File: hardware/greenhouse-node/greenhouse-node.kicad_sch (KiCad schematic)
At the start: 30 parts, among them J1 Conn_01x12_Male, J2 Conn_01x02_Male, J3 Conn_01x02_Male, J4 Conn_01x02_Male, J5 Conn_01x04_Male, J6 RX_PinHeader_1x04_P2.54mm, J7 TX_PinHeader_1x04_P2.54mm, Q1 BC549C, U1 ATtiny84A-P, U2 L7805, U3 74HC595

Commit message: Swap OE and RCLK
Drive OE low
Fixed missing SRCLR pull-up
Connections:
- net SR_OE: now also U1.6 (PA7); no longer J5.4 (Pin_4), U1.9 (PA4)
- net SR_RCLK: now also J5.4 (Pin_4), U1.9 (PA4); no longer U1.6 (PA7)
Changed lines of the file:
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@@
     (stroke (width 0) (type default) (color 0 0 0 0))
   )
-  (wire (pts (xy 116.84 99.06) (xy 134.62 99.06))
+  (wire (pts (xy 134.62 97.79) (xy 134.62 100.33))
+    (stroke (width 0) (type default) (color 0 0 0 0))
+  )
+  (wire (pts (xy 116.84 106.68) (xy 134.62 106.68))
     (stroke (width 0) (type default) (color 0 0 0 0))
   )
@@
     (stroke (width 0) (type default) (color 0 0 0 0))
   )
-  (wire (pts (xy 123.19 154.94) (xy 130.81 154.94))
+  (wire (pts (xy 123.19 154.94) (xy 133.35 154.94))
     (stroke (width 0) (type default) (color 0 0 0 0))
   )
@@
     (stroke (width 0) (type default) (color 0 0 0 0))
   )
-  (wire (pts (xy 123.19 147.32) (xy 130.81 147.32))
+  (wire (pts (xy 123.19 147.32) (xy 133.35 147.32))
     (stroke (width 0) (type default) (color 0 0 0 0))
   )
@@
     (stroke (width 0) (type default) (color 0 0 0 0))
   )
+  (wire (pts (xy 116.84 99.06) (xy 130.81 99.06))
+    (stroke (width 0) (type default) (color 0 0 0 0))
+  )
   (wire (pts (xy 116.84 104.14) (xy 130.81 104.14))
     (stroke (width 0) (type default) (color 0 0 0 0))
@@
     (stroke (width 0) (type default) (color 0 0 0 0))
   )
-  (wire (pts (xy 134.62 90.17) (xy 134.62 92.71))
-    (stroke (width 0) (type default) (color 0 0 0 0))
-  )
-  (wire (pts (xy 116.84 106.68) (xy 130.81 106.68))
-    (stroke (width 0) (type default) (color 0 0 0 0))
-  )
   (wire (pts (xy 57.15 97.79) (xy 57.15 105.41))
     (stroke (width 0) (type default) (color 0 0 0 0))
@@
     (stroke (width 0) (type default) (color 0 0 0 0))
   )
-  (wire (pts (xy 134.62 97.79) (xy 134.62 99.06))
-    (stroke (width 0) (type default) (color 0 0 0 0))
-  )
   (wire (pts (xy 100.33 52.07) (xy 106.68 52.07))
     (stroke (width 0) (type default) (color 0 0 0 0))
@@
     (stroke (width 0) (type default) (color 0 0 0 0))
   )
-  (wire (pts (xy 123.19 152.4) (xy 130.81 152.4))
+  (wire (pts (xy 123.19 152.4) (xy 133.35 152.4))
     (stroke (width 0) (type default) (color 0 0 0 0))
   )
@@
     (stroke (width 0) (type default) (color 0 0 0 0))
   )
-  (wire (pts (xy 123.19 149.86) (xy 130.81 149.86))
+  (wire (pts (xy 134.62 105.41) (xy 134.62 106.68))
+    (stroke (width 0) (type default) (color 0 0 0 0))
+  )
+  (wire (pts (xy 123.19 149.86) (xy 133.35 149.86))
     (stroke (width 0) (type default) (color 0 0 0 0))
   )
@@
     (effects (font (size 1.27 1.27)) (justify right bottom))
   )
-  (label "SR_SER" (at 130.81 149.86 180)
-    (effects (font (size 1.27 1.27)) (justify right bottom))
-  )
-  (label "SR_OE" (at 130.81 154.94 180)
+  (label "SR_OE" (at 130.81 106.68 180)
+    (effects (font (size 1.27 1.27)) (justify right bottom))
+  )
+  (label "SR_SER" (at 133.35 149.86 180)
+    (effects (font (size 1.27 1.27)) (justify right bottom))
+  )
+  (label "SR_RCLK" (at 133.35 154.94 180)
     (effects (font (size 1.27 1.27)) (justify right bottom))
   )
@@
     (effects (font (size 1.27 1.27)) (justify right bottom))
   )
-  (label "SR_CLK" (at 130.81 152.4 180)
+  (label "SR_RCLK" (at 130.81 99.06 180)
+    (effects (font (size 1.27 1.27)) (justify right bottom))
+  )
+  (label "SR_CLK" (at 133.35 152.4 180)
     (effects (font (size 1.27 1.27)) (justify right bottom))
   )
@@
     (effects (font (size 1.27 1.27)) (justify left bottom))
   )
-  (label "SR_OE" (at 130.81 99.06 180)
-    (effects (font (size 1.27 1.27)) (justify right bottom))
-  )
   (label "RAD_TX" (at 228.6 53.34 0)
     (effects (font (size 1.27 1.27)) (justify left bottom))
@@
     (effects (font (size 1.27 1.27)) (justify right bottom))
   )
-  (label "SR_RCLK" (at 130.81 106.68 180)
-    (effects (font (size 1.27 1.27)) (justify right bottom))
-  )
   (label "LED_Y" (at 152.4 53.34 0)
     (effects (font (size 1.27 1.27)) (justify left bottom))
@@
     (effects (font (size 1.27 1.27)) (justify right bottom))
   )
-  (label "Reset" (at 130.81 147.32 180)
+  (label "Reset" (at 133.35 147.32 180)
     (effects (font (size 1.27 1.27)) (justify right bottom))
   )
@@
     (pin "2")
   )
+  (symbol (lib_id "power:+5V") (at 134.62 97.79 0) (mirror y) (unit 1)
+    (in_bom yes) (on_board yes) (fields_autoplaced)
+    (property "Reference" "#PWR014" (id 0) (at 134.62 101.6 0)
+      (effects (font (size 1.27 1.27)) hide)
+    )
+    (property "Value" "+5V" (id 1) (at 134.62 92.71 0))
+    (property "Footprint" "" (id 2) (at 134.62 97.79 0)
+      (effects (font (size 1.27 1.27)) hide)
+    )
+    (property "Datasheet" "" (id 3) (at 134.62 97.79 0)
+      (effects (font (size 1.27 1.27)) hide)
+    )
+    (pin "1")
+  )
   (symbol (lib_id "Regulator_Linear:L7805") (at 106.68 43.18 0) (unit 1)
     (in_bom yes) (on_board yes) (fields_autoplaced)
@@
     (pin "1")
   )
-  (symbol (lib_id "Device:R_Small_US") (at 134.62 95.25 0) (mirror y) (unit 1)
-    (in_bom yes) (on_board yes) (fields_autoplaced)
-    (property "Reference" "R2" (id 0) (at 137.16 93.9799 0)
-      (effects (font (size 1.27 1.27)) (justify right))
-    )
-    (property "Value" "5k" (id 1) (at 137.16 96.5199 0)
-      (effects (font (size 1.27 1.27)) (justify right))
-    )
-    (property "Footprint" "Resistor_THT:R_Axial_DIN0204_L3.6mm_D1.6mm_P7.62mm_Horizontal" (id 2) (at 134.62 95.25 0)
-      (effects (font (size 1.27 1.27)) hide)
-    )
-    (property "Datasheet" "~" (id 3) (at 134.62 95.25 0)
-      (effects (font (size 1.27 1.27)) hide)
-    )
-    (pin "1")
-    (pin "2")
-  )
   (symbol (lib_id "Device:C_Small") (at 97.79 52.07 270) (unit 1)
     (in_bom yes) (on_board yes) (fields_autoplaced)
@@
     (pin "1")
     (pin "2")
-  )
-  (symbol (lib_id "power:+5V") (at 134.62 90.17 0) (mirror y) (unit 1)
-    (in_bom yes) (on_board yes) (fields_autoplaced)
-    (property "Reference" "#PWR014" (id 0) (at 134.62 93.98 0)
-      (effects (font (size 1.27 1.27)) hide)
-    )
-    (property "Value" "+5V" (id 1) (at 134.62 85.09 0))
-    (property "Footprint" "" (id 2) (at 134.62 90.17 0)
-      (effects (font (size 1.27 1.27)) hide)
-    )
-    (property "Datasheet" "" (id 3) (at 134.62 90.17 0)
-      (effects (font (size 1.27 1.27)) hide)
-    )
-    (pin "1")
   )
   (symbol (lib_id "power:+10V") (at 60.96 30.48 0) (unit 1)
@@
     (pin "4")
   )
+  (symbol (lib_id "Device:R_Small_US") (at 134.62 102.87 0) (mirror y) (unit 1)
+    (in_bom yes) (on_board yes) (fields_autoplaced)
+    (property "Reference" "R2" (id 0) (at 137.16 101.5999 0)
+      (effects (font (size 1.27 1.27)) (justify right))
+    )
+    (property "Value" "5k" (id 1) (at 137.16 104.1399 0)
+      (effects (font (size 1.27 1.27)) (justify right))
+    )
+    (property "Footprint" "Resistor_THT:R_Axial_DIN0204_L3.6mm_D1.6mm_P7.62mm_Horizontal" (id 2) (at 134.62 102.87 0)
+      (effects (font (size 1.27 1.27)) hide)
+    )
+    (property "Datasheet" "~" (id 3) (at 134.62 102.87 0)
+      (effects (font (size 1.27 1.27)) hide)
+    )
+    (pin "1")
+    (pin "2")
+  )
   (symbol (lib_id "power:+5V") (at 218.44 39.37 0) (mirror y) (unit 1)
     (in_bom yes) (on_board yes) (fields_autoplaced)
@@
       (reference "#PWR013") (unit 1) (value "+5V") (footprint "")
     )
-    (path "/86dc60dd-744c-44c7-a7c5-a11274a23f7e"
+    (path "/079bd503-9dc1-457f-9fb1-9d8247e28272"
       (reference "#PWR014") (unit 1) (value "+5V") (footprint "")
     )
@@
       (reference "R1") (unit 1) (value "5k") (footprint "Resistor_THT:R_Axial_DIN0204_L3.6mm_D1.6mm_P7.62mm_Horizontal")
     )
-    (path "/302b2aa9-738c-4aa7-b455-5a902820fe10"
+    (path "/d2752f88-c4a3-4e40-8284-9dc4aea70bf3"
       (reference "R2") (unit 1) (value "5k") (footprint "Resistor_THT:R_Axial_DIN0204_L3.6mm_D1.6mm_P7.62mm_Horizontal")
     )

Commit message: Add cap and diode
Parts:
- added C1: 100uF, Capacitor_THT:C_Radial_D5.0mm_H7.0mm_P2.00mm, symbol Device:C_Small
- added D1: D, Diode_THT:D_A-405_P7.62mm_Horizontal, symbol Device:D
- renumbered C1 to C2, C2 to C3, C3 to C4, C4 to C5, D1 to D2, D2 to D3, D3 to D4, D4 to D5
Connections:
- net +10V: now also D1.2 (A); no longer C3.2, U2.1 (IN)
- net +5V: now also C1.1
- net GND: now also C1.2
- new net: C3.2, D1.1 (K), U2.1 (IN)

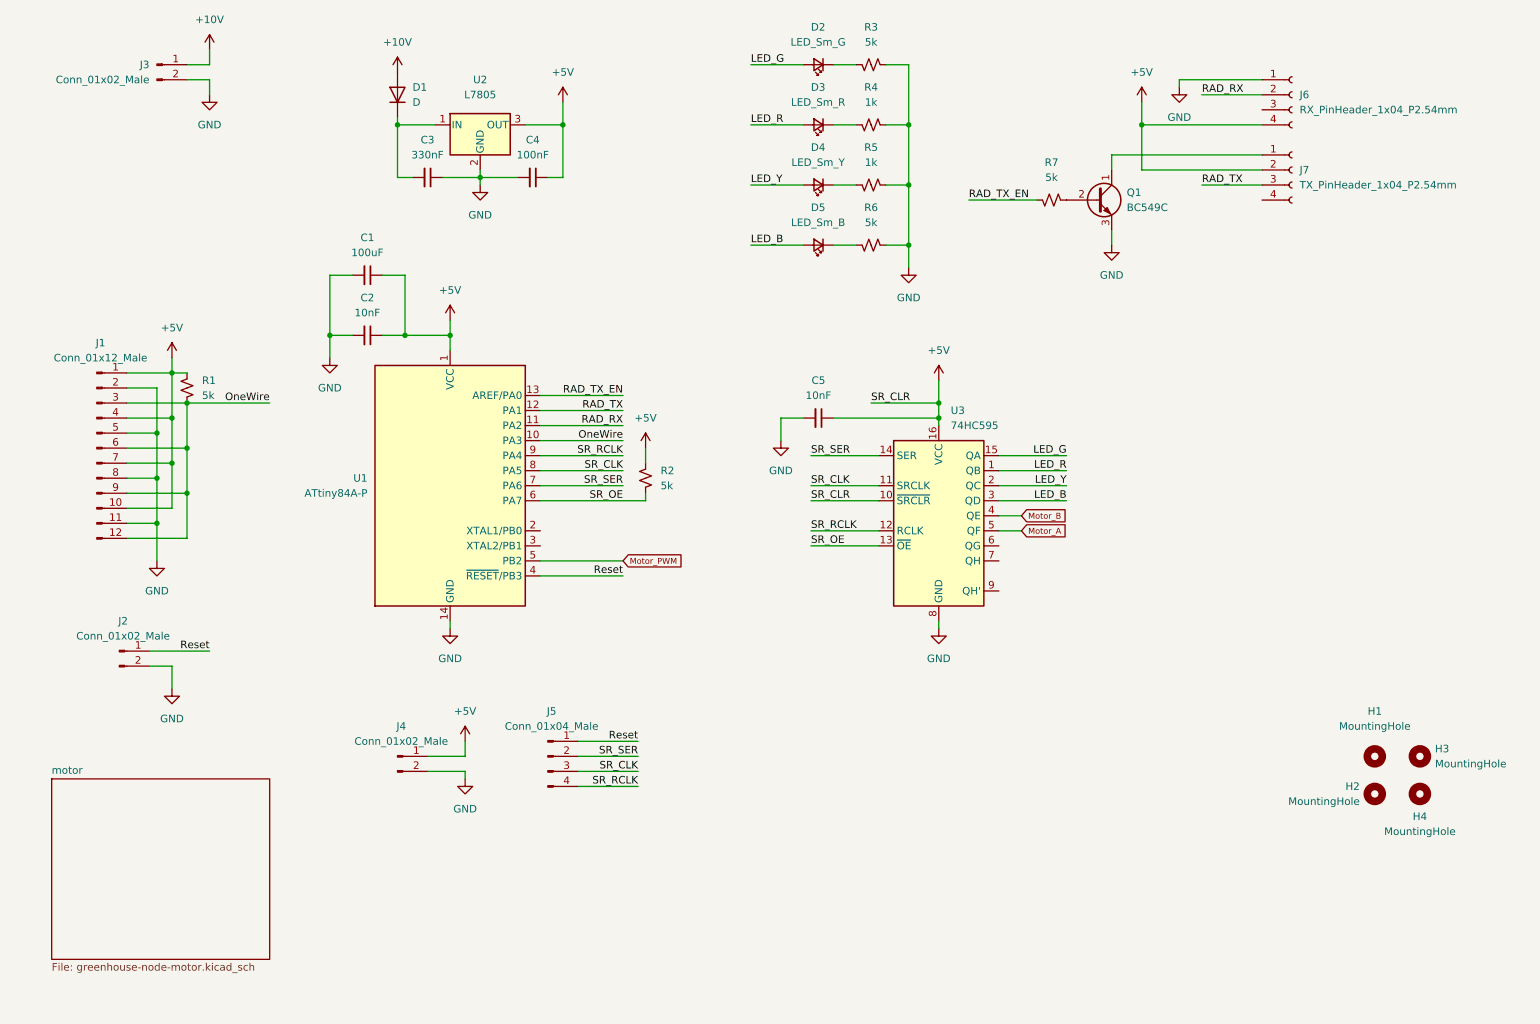
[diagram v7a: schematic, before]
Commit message: Add crystal to node board
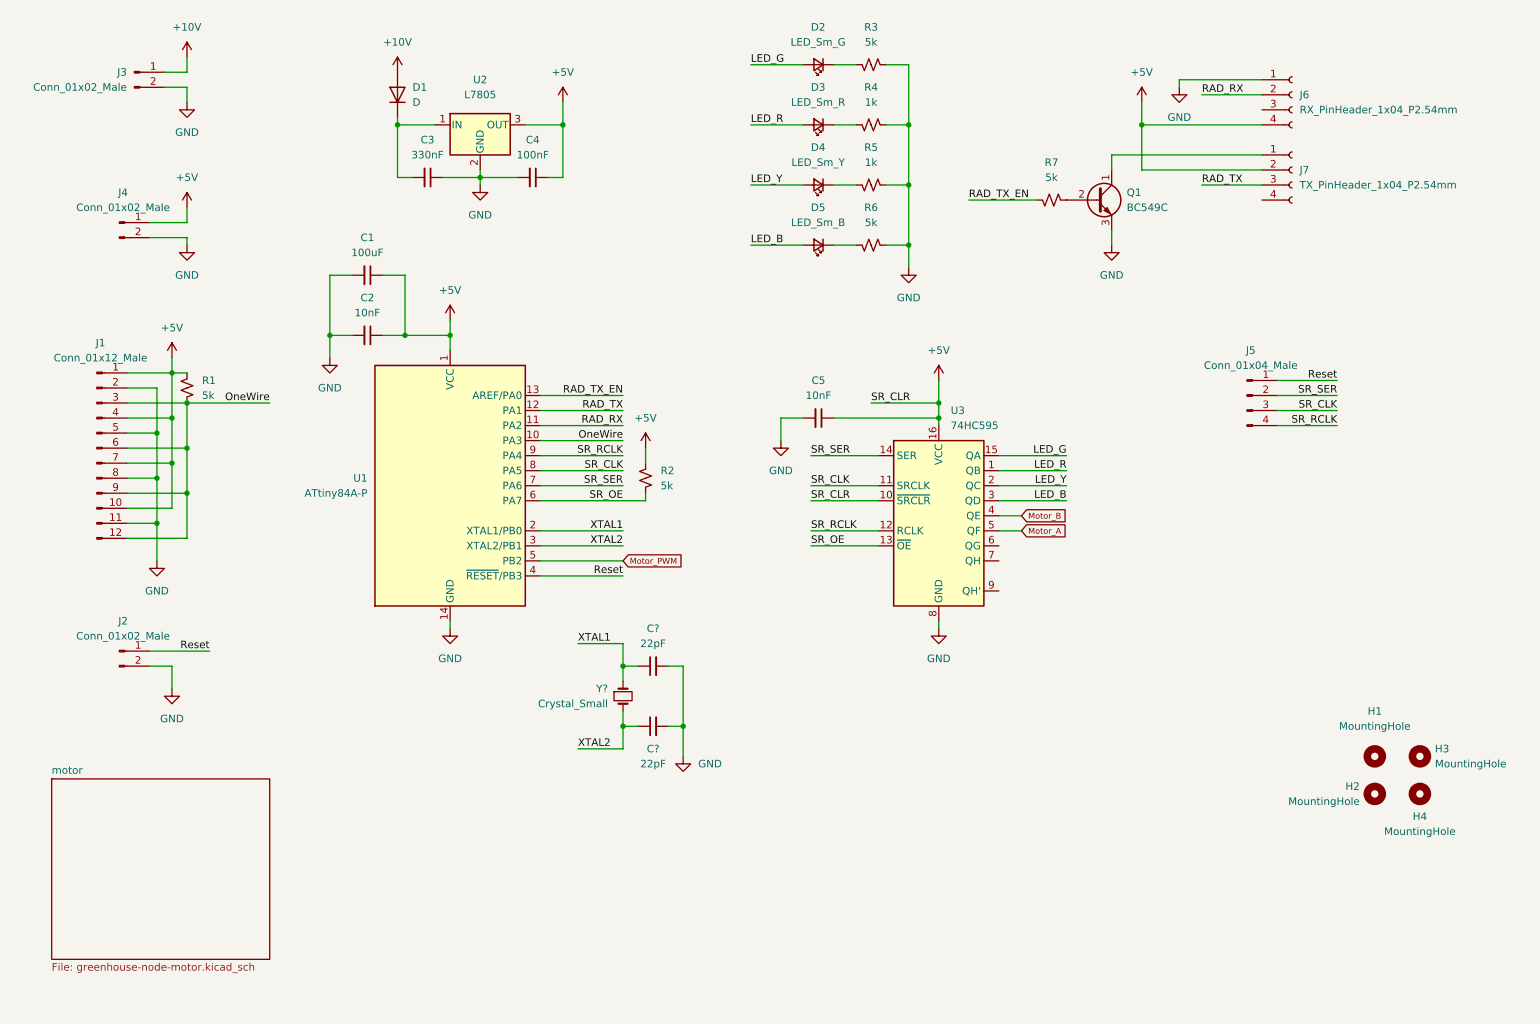
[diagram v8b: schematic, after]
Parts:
- added C? (x2): 22pF, Capacitor_THT:C_Disc_D4.7mm_W2.5mm_P5.00mm, symbol Device:C_Small
- added Y?: Crystal_Small, symbol Device:Crystal_Small
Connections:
- net GND: now also C?.2, C?.2
- net XTAL1: now reaches U1.2 (XTAL1/PB0)
- net XTAL1: now also C?.1, Y?.1
- net XTAL2: now reaches U1.3 (XTAL2/PB1)
- net XTAL2: now also C?.1, Y?.2
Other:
- moved on the sheet: J3, J4, J5
